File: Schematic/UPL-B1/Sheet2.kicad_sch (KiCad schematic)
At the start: 40 parts, among them K2 G5V-2_Split, P20 TestPoint, P21 TestPoint, X2 Conn_01x03_Pin_Bridge

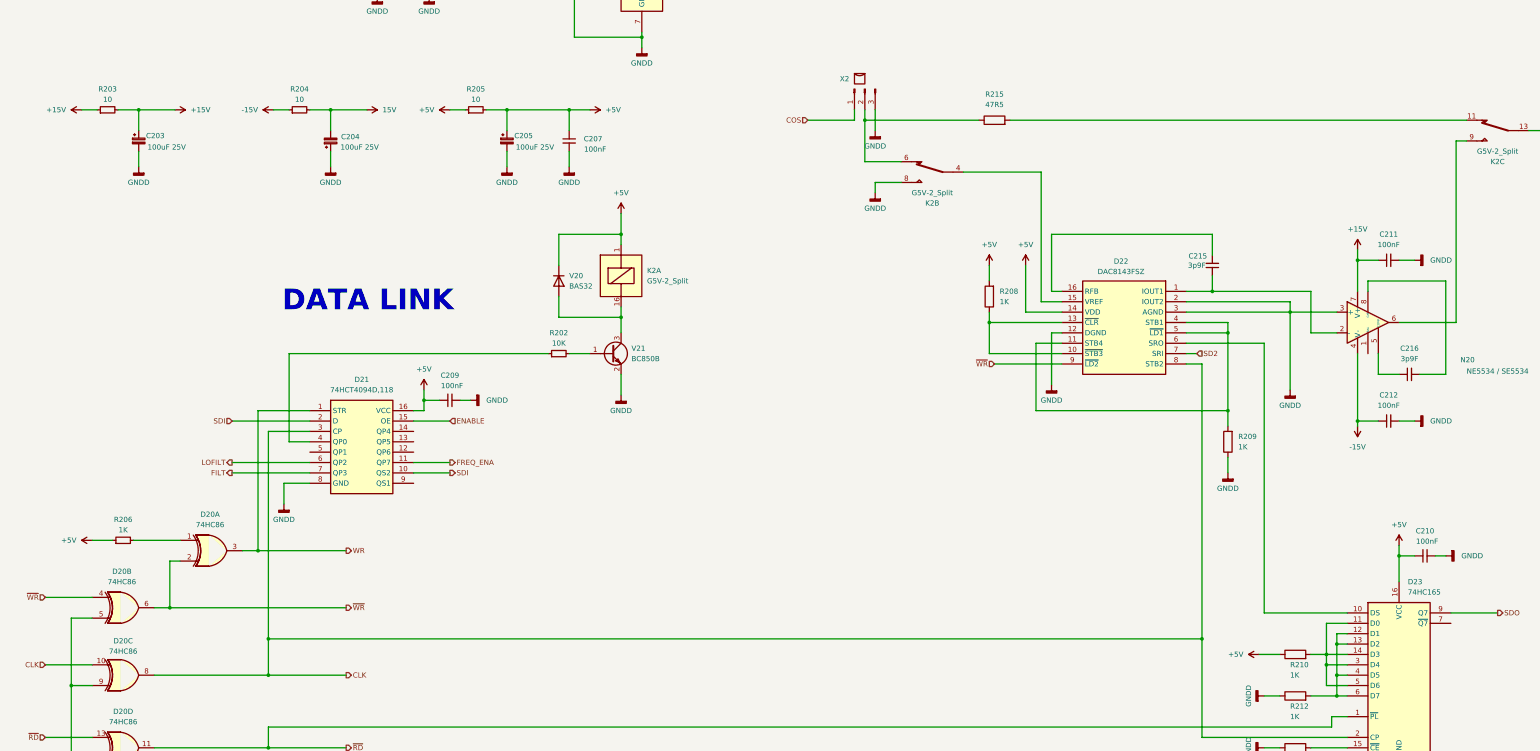
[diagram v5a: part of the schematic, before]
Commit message: Updated symbols for ADC and Shiftregister
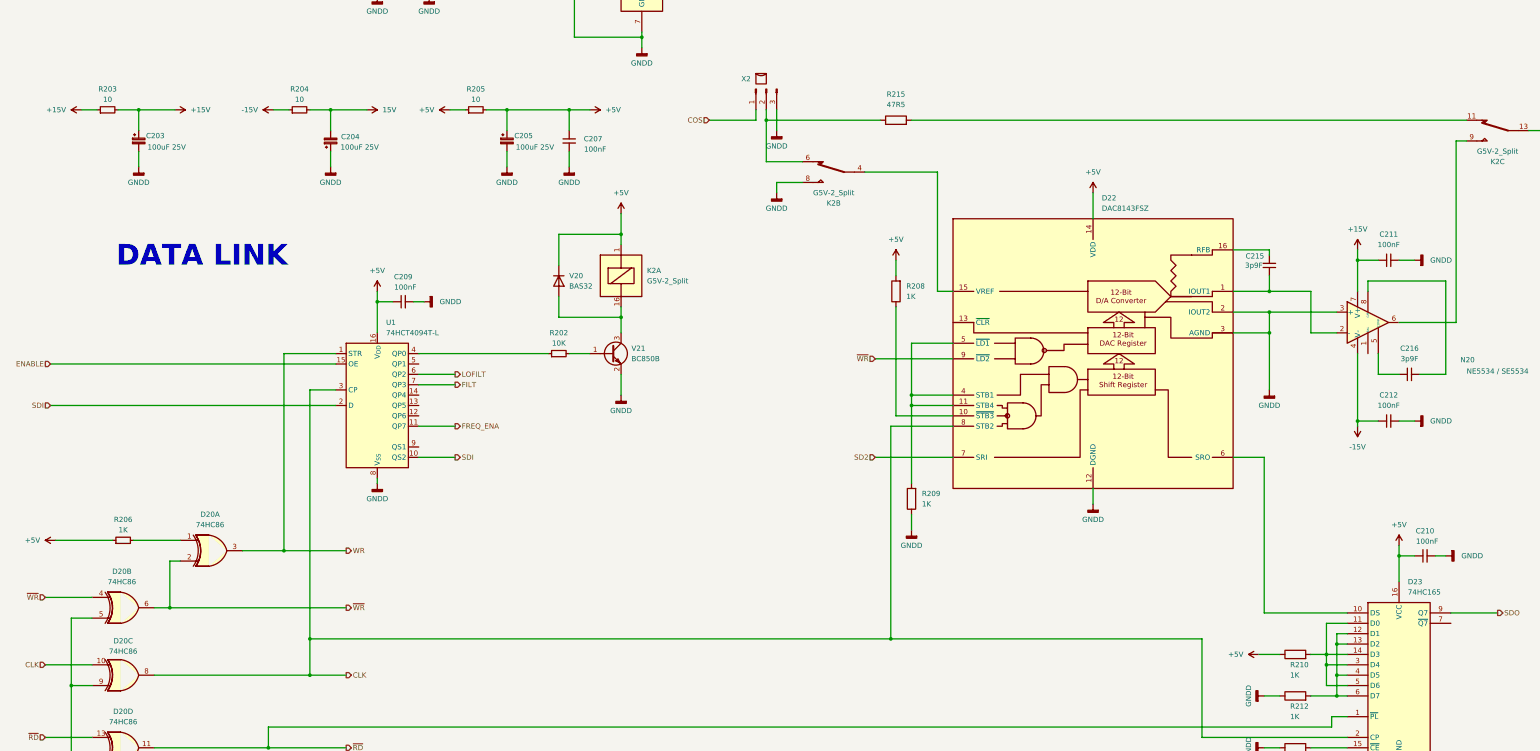
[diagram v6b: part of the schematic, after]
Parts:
- removed D21: 74HCT4094D,118, 74HCT4094D118, symbol UPL_B1:74HCT4094D,118
- removed D22: DAC8143FSZ, SOIC127P1032X265-16N, symbol UPL_B1:DAC8143FSZ
- added D22: DAC8143FSZ, SOIC127P1032X265-16N, symbol UPL_B1:DAC8143FSZ_
- added U1: 74HCT4094T-L, Package_SO:SOIC-16_3.9x9.9mm_P1.27mm, symbol UPL_B1:74HCT4094T-L
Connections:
- net +5V: now also D22.14 (VDD), U1.16 (V_{DD})
- net CLK: now also D22.8 (STB2), U1.3 (CP)
- net ENABLE: now also U1.15 (OE)
- net FILT: now also U1.7 (QP3)
- net FREQ_ENA: now also U1.11 (QP7)
- net GNDD: now also D22.12 (DGND), D22.2 (IOUT2), D22.3 (AGND), U1.8 (V_{SS})
- net LOFILT: now also U1.6 (QP2)
- net SD2: now also D22.7 (SRI)
- net SDI: now also U1.10 (QS2), U1.2 (D)
- net WR: now also U1.1 (STR)
- net ~{WR}: now also D22.9 (~{LD2})
- net at R208.1: now also D22.10 (~{STB3})
- net at C215.1, N20.2 (-): now also D22.1 (IOUT1)
- net at R209.2: now also D22.11 (STB4), D22.4 (STB1), D22.5 (~{LD1})
- net at K2.4: now also D22.15 (VREF)
- net at C215.2: now also D22.16 (RFB)
- net at D23.10 (DS): now also D22.6 (SRO)
- net at R202.1: now also U1.4 (QP0)
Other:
- moved on the sheet: C209, C215, K2B, R208, R209, R215, X2

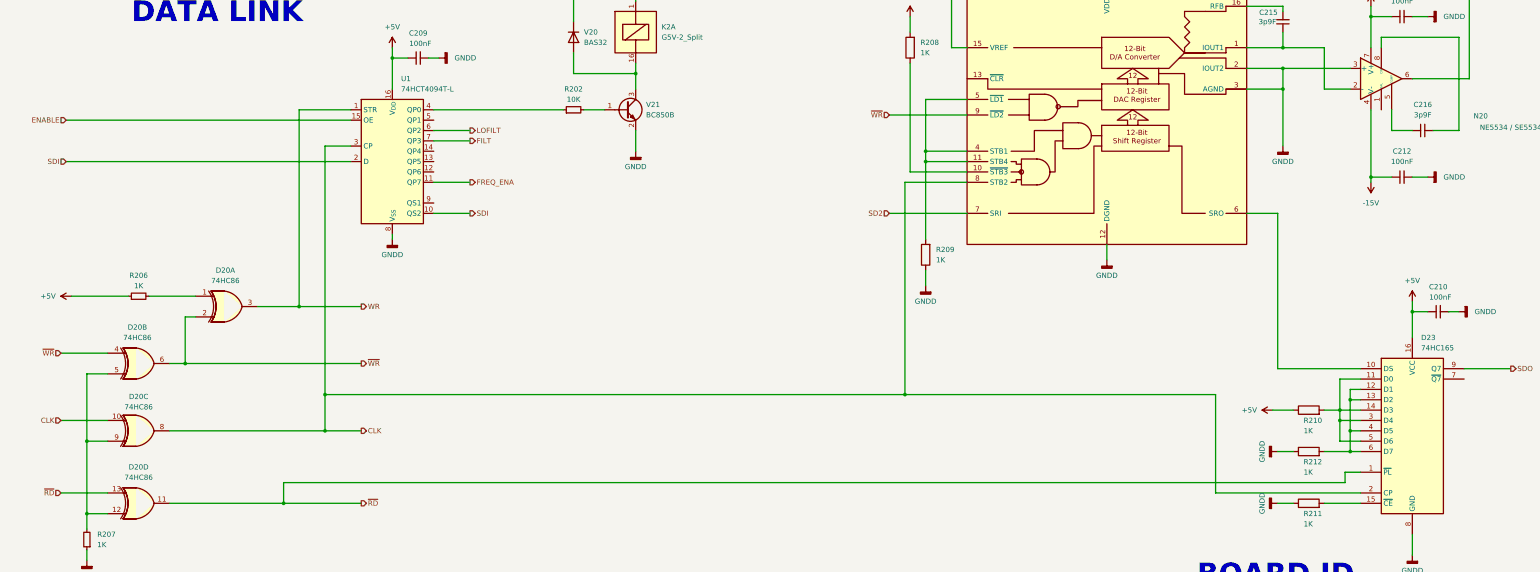
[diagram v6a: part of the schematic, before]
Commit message: Group functional blocks in ALC. Begin documenting digital chain.
Fixed D21 designator, placed a few NC-Crosses on unused pins for good
practice.
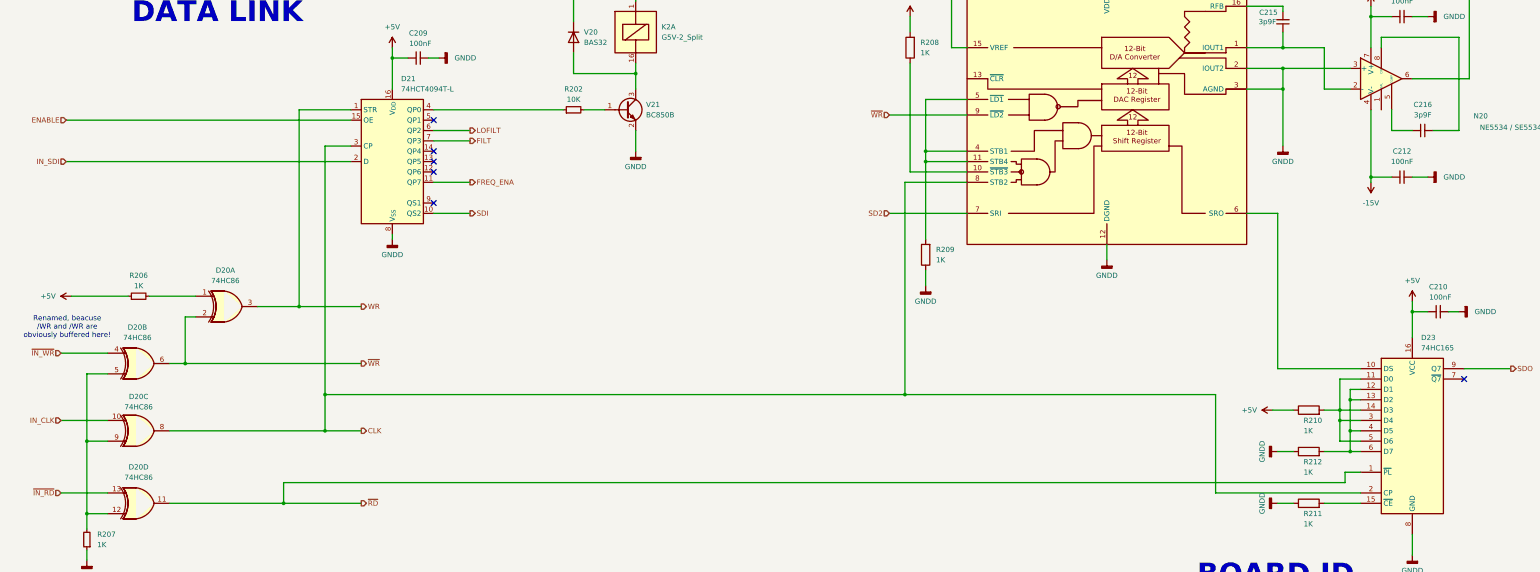
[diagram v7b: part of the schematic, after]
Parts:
- renumbered U1 to D21
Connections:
- net CLK: no longer D20.10
- net SDI: no longer D21.2 (D)
- net ~{RD}: no longer D20.13
- net ~{WR}: no longer D20.4
- new net IN_CLK: D20.10
- new net IN_SDI: D21.2 (D)
- new net ~{IN_RD}: D20.13
- new net ~{IN_WR}: D20.4
- no-connect marks 0 -> 6
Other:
- note added: "Renamed, beacuse /WR and /WR are obviously buffered here!"
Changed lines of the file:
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@@
 		(company "BVKSound")
 	)
+	(text "Renamed, beacuse \n/WR and /WR are \nobviously buffered here!"
+		(exclude_from_sim no)
+		(at 24.384 182.88 0)
+		(effects
+			(font
+				(size 1.27 1.27)
+			)
+		)
+	)
 	(text "IMD ATTEN"
 		(exclude_from_sim no)
@@
 		(color 0 0 0 0)
 	)
+	(no_connect
+		(at 367.03 195.58)
+	)
+	(no_connect
+		(at 114.3 142.24)
+	)
+	(no_connect
+		(at 114.3 132.08)
+	)
+	(no_connect
+		(at 114.3 144.78)
+	)
+	(no_connect
+		(at 114.3 139.7)
+	)
+	(no_connect
+		(at 114.3 152.4)
+	)
 	(wire
 		(pts
@@
 		)
 	)
-	(hierarchical_label "~{WR}"
+	(hierarchical_label "~{IN_WR}"
 		(shape input)
 		(at 22.86 189.23 180)
@@
 		)
 	)
-	(hierarchical_label "SDI"
+	(hierarchical_label "IN_SDI"
 		(shape input)
 		(at 24.13 142.24 180)
@@
 		)
 	)
-	(hierarchical_label "~{RD}"
+	(hierarchical_label "~{IN_RD}"
 		(shape input)
 		(at 22.86 223.52 180)
@@
 		)
 	)
-	(hierarchical_label "CLK"
+	(hierarchical_label "IN_CLK"
 		(shape input)
 		(at 22.86 205.74 180)
@@
 		(dnp no)
 		(fields_autoplaced yes)
-		(property "Reference" "U1"
+		(property "Reference" "D21"
 			(at 106.2833 121.92 0)
 			(effects
@@
 			(project ""
 				(path "/812de09b-8b67-463d-bf96-bb3aeeb1ed8d/daa8f8c7-f164-4600-9939-51b125d2037c"
-					(reference "U1")
+					(reference "D21")
 					(unit 1)
 				)

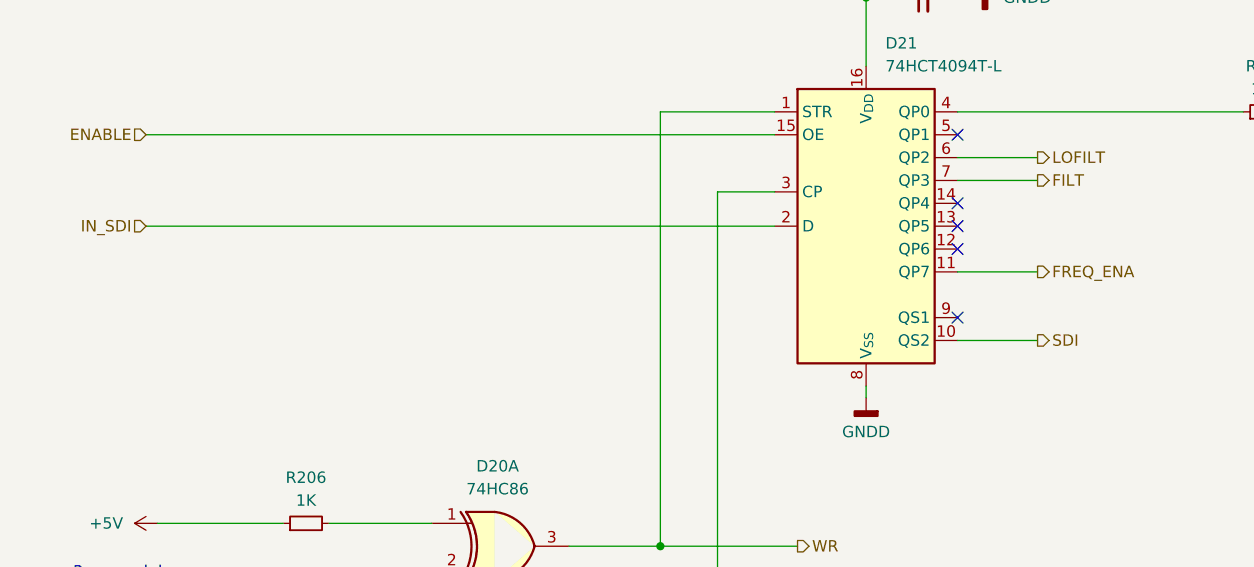
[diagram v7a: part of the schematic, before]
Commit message: Rework digital signal chain
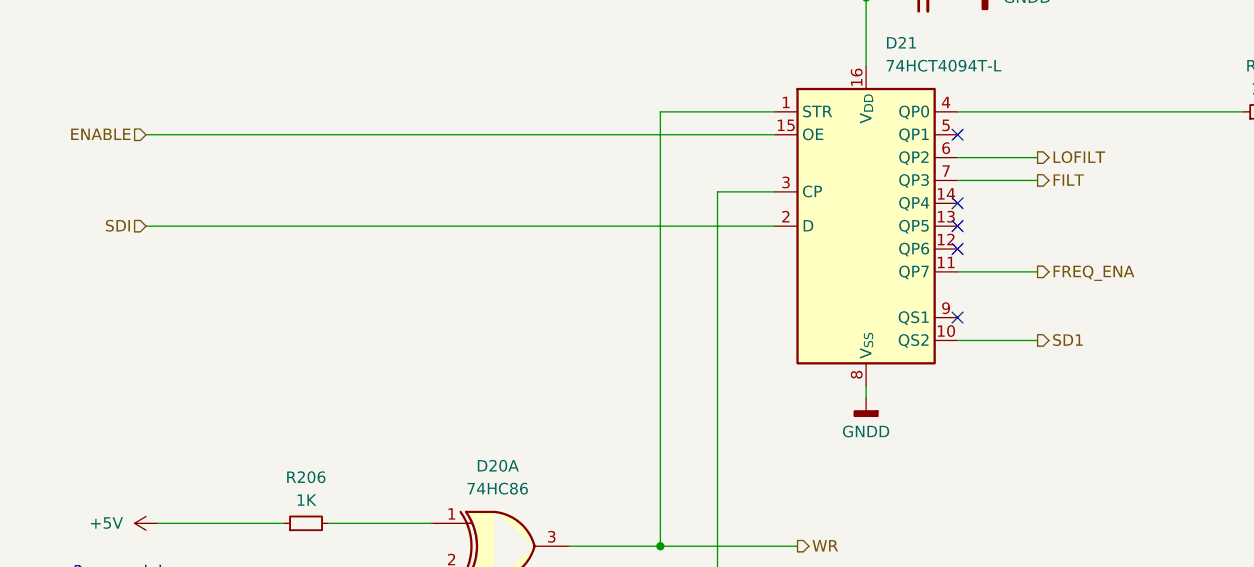
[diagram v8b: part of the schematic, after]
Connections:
- net IN_SDI is gone; now on net SDI: D21.2 (D)
- net SDI: no longer D21.10 (QS2)
- new net SD1: D21.10 (QS2)
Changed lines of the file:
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@@
 		)
 	)
-	(hierarchical_label "IN_SDI"
+	(hierarchical_label "SDI"
 		(shape input)
 		(at 24.13 142.24 180)
@@
 		)
 	)
-	(hierarchical_label "SDI"
+	(hierarchical_label "SD1"
 		(shape output)
 		(at 123.19 154.94 0)
